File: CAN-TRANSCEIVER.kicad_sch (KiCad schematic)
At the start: 16 parts, among them U7 ATA6561-GAQW-N

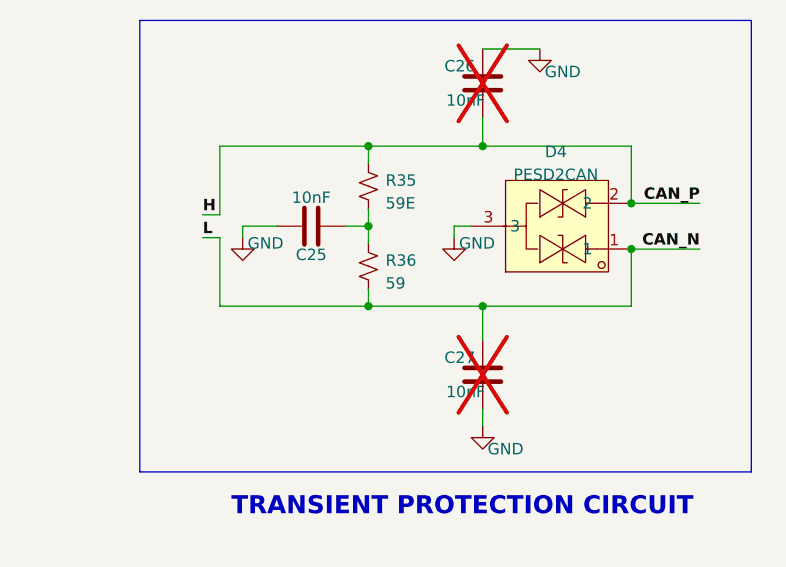
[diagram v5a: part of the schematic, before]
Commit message: Added production files for JLC (BOM and CPL)
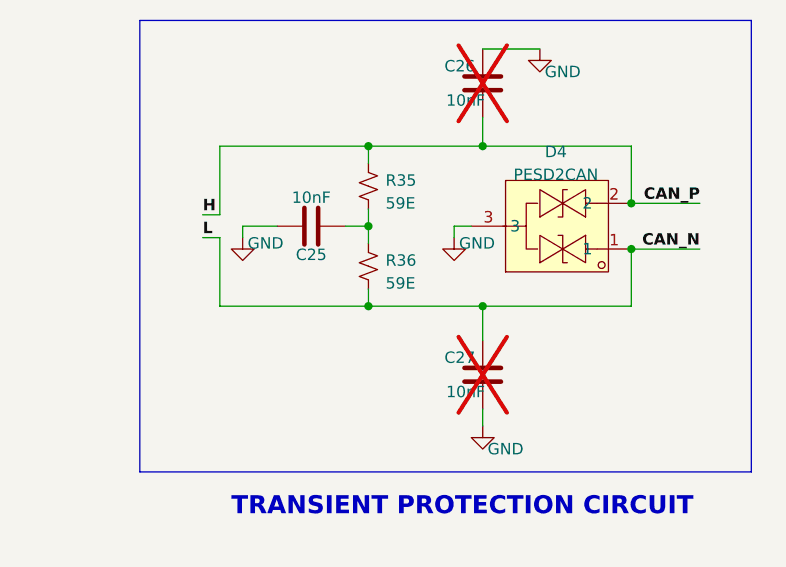
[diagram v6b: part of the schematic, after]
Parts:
- C23, C24: LCSC Part Number (none) -> C2173920
- C25: LCSC Part Number (none) -> C458948; PN CC0402KRX7R9BB103 -> MT15B103K250CT
- C26, C27: LCSC Part Number (none) -> C327415
- D4: LCSC Part Number (none) -> C284078
- R14: LCSC Part Number (none) -> C95177
- R34: LCSC Part Number (none) -> C105872
- R35: LCSC Part Number (none) -> C273340
- R36: value 59 -> 59E; LCSC Part Number (none) -> C273340
- R37, R38: LCSC Part Number (none) -> C102753
- TP3, TP4, TP6: now left out of the parts list
- U7: LCSC Part Number (none) -> C616016
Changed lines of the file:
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@@
+      (effects (font (size 1.27 1.27)) hide)
+    )
+    (property "LCSC Part Number" "C2173920" (at 166.37 110.49 0)
       (effects (font (size 1.27 1.27)) hide)
     )
@@
       (effects (font (size 1.27 1.27)) hide)
     )
+    (property "LCSC Part Number" "C2173920" (at 127.635 110.49 0)
+      (effects (font (size 1.27 1.27)) hide)
+    )
     (pin "1")
     (pin "2")
@@
   )
   (symbol (lib_id "ESP32-S3_DB:TestPoint_Alt") (at 55.245 101.6 0) (unit 1)
-    (in_bom yes) (on_board yes) (dnp no)
+    (in_bom no) (on_board yes) (dnp no)
     (property "Reference" "TP4" (at 50.8 98.425 0)
       (effects (font (size 1.27 1.27)) (justify left))
@@
       (effects (font (size 1.27 1.27)) hide)
     )
+    (property "Sim.Enable" "0" (at 55.245 101.6 0)
+      (effects (font (size 1.27 1.27)) hide)
+    )
     (pin "1")
     (instances
@@
     )
     (property "PN" "RC0402FR-075K1L" (at 165.735 92.075 0)
+      (effects (font (size 1.27 1.27)) hide)
+    )
+    (property "LCSC Part Number" "C105872" (at 165.735 92.075 0)
       (effects (font (size 1.27 1.27)) hide)
     )
@@
       (effects (font (size 1.27 1.27)) hide)
     )
+    (property "LCSC Part Number" "C327415" (at 239.395 80.645 0)
+      (effects (font (size 1.27 1.27)) hide)
+    )
     (pin "1")
     (pin "2")
@@
       (effects (font (size 1.27 1.27)) hide)
     )
+    (property "LCSC Part Number" "C95177" (at 123.825 100.965 0)
+      (effects (font (size 1.27 1.27)) hide)
+    )
     (pin "1")
     (pin "2")
@@
   )
   (symbol (lib_id "ESP32-S3_DB:TestPoint_Alt") (at 48.895 84.455 0) (unit 1)
-    (in_bom yes) (on_board yes) (dnp no)
+    (in_bom no) (on_board yes) (dnp no)
     (property "Reference" "TP6" (at 44.45 81.28 0)
       (effects (font (size 1.27 1.27)) (justify left))
@@
       (effects (font (size 1.27 1.27)) hide)
     )
+    (property "Sim.Enable" "0" (at 48.895 84.455 0)
+      (effects (font (size 1.27 1.27)) hide)
+    )
     (pin "1")
     (instances
@@
         (path "/b7fc4bd3-c219-4455-832b-8d795385dcf1/5968696a-d1c3-4df1-9868-cceeab327a7d"
           (reference "#PWR039") (unit 1)
-        )
-      )
-    )
-  )
-  (symbol (lib_id "ESP32-S3_DB:R_Small_US") (at 226.695 100.965 180) (unit 1)
-    (in_bom yes) (on_board yes) (dnp no) (fields_autoplaced)
-    (property "Reference" "R36" (at 228.6 100.33 0)
-      (effects (font (size 1.27 1.27)) (justify right))
-    )
-    (property "Value" "59" (at 228.6 102.87 0)
-      (effects (font (size 1.27 1.27)) (justify right))
-    )
-    (property "Footprint" "ESP32-S3_Dev_Board:R_0402_1005Metric" (at 226.695 100.965 0)
-      (effects (font (size 1.27 1.27)) hide)
-    )
-    (property "Datasheet" "~" (at 226.695 100.965 0)
-      (effects (font (size 1.27 1.27)) hide)
-    )
-    (property "PN" "RC0402FR-0759RL" (at 226.695 100.965 0)
-      (effects (font (size 1.27 1.27)) hide)
-    )
-    (pin "1")
-    (pin "2")
-    (instances
-      (project "ESP32-S3_DB"
-        (path "/b7fc4bd3-c219-4455-832b-8d795385dcf1/5968696a-d1c3-4df1-9868-cceeab327a7d"
-          (reference "R36") (unit 1)
         )
       )
@@
     )
     (property "PN" "ATA6561-GAQW-N" (at 134.62 95.885 0)
+      (effects (font (size 1.27 1.27)) hide)
+    )
+    (property "LCSC Part Number" "C616016" (at 134.62 95.885 0)
       (effects (font (size 1.27 1.27)) hide)
     )
@@
       (effects (font (size 1.27 1.27)) hide)
     )
+    (property "LCSC Part Number" "C284078" (at 248.285 96.52 0)
+      (effects (font (size 1.27 1.27)) hide)
+    )
     (pin "1")
     (pin "2")
@@
     )
   )
+  (symbol (lib_id "ESP32-S3_DB:R_Small_US") (at 226.695 100.965 180) (unit 1)
+    (in_bom yes) (on_board yes) (dnp no) (fields_autoplaced)
+    (property "Reference" "R36" (at 228.6 100.33 0)
+      (effects (font (size 1.27 1.27)) (justify right))
+    )
+    (property "Value" "59E" (at 228.6 102.87 0)
+      (effects (font (size 1.27 1.27)) (justify right))
+    )
+    (property "Footprint" "ESP32-S3_Dev_Board:R_0402_1005Metric" (at 226.695 100.965 0)
+      (effects (font (size 1.27 1.27)) hide)
+    )
+    (property "Datasheet" "~" (at 226.695 100.965 0)
+      (effects (font (size 1.27 1.27)) hide)
+    )
+    (property "PN" "RC0402FR-0759RL" (at 226.695 100.965 0)
+      (effects (font (size 1.27 1.27)) hide)
+    )
+    (property "LCSC Part Number" "C273340" (at 226.695 100.965 0)
+      (effects (font (size 1.27 1.27)) hide)
+    )
+    (pin "1")
+    (pin "2")
+    (instances
+      (project "ESP32-S3_DB"
+        (path "/b7fc4bd3-c219-4455-832b-8d795385dcf1/5968696a-d1c3-4df1-9868-cceeab327a7d"
+          (reference "R36") (unit 1)
+        )
+      )
+    )
+  )
   (symbol (lib_id "ESP32-S3_DB:TestPoint_Alt") (at 55.245 95.25 0) (unit 1)
-    (in_bom yes) (on_board yes) (dnp no)
+    (in_bom no) (on_board yes) (dnp no)
     (property "Reference" "TP3" (at 50.8 92.075 0)
       (effects (font (size 1.27 1.27)) (justify left))
@@
       (effects (font (size 1.27 1.27)) hide)
     )
+    (property "Sim.Enable" "0" (at 55.245 95.25 0)
+      (effects (font (size 1.27 1.27)) hide)
+    )
     (pin "1")
     (instances
@@
       (effects (font (size 1.27 1.27)) hide)
     )
+    (property "LCSC Part Number" "C102753" (at 66.04 101.6 0)
+      (effects (font (size 1.27 1.27)) hide)
+    )
     (pin "1")
     (pin "2")
@@
     )
     (property "PN" "RTT02100JTH" (at 66.04 95.25 0)
+      (effects (font (size 1.27 1.27)) hide)
+    )
+    (property "LCSC Part Number" "C102753" (at 66.04 95.25 0)
       (effects (font (size 1.27 1.27)) hide)
     )
@@
       (effects (font (size 1.27 1.27)) hide)
     )
+    (property "LCSC Part Number" "C273340" (at 226.695 92.075 0)
+      (effects (font (size 1.27 1.27)) hide)
+    )
     (pin "1")
     (pin "2")
@@
       (effects (font (size 1.27 1.27)) hide)
     )
-    (property "PN" "CC0402KRX7R9BB103" (at 220.345 96.52 0)
+    (property "PN" "MT15B103K250CT" (at 220.345 96.52 0)
+      (effects (font (size 1.27 1.27)) hide)
+    )
+    (property "LCSC Part Number" "C458948" (at 220.345 96.52 0)
       (effects (font (size 1.27 1.27)) hide)
     )
@@
       (effects (font (size 1.27 1.27)) hide)
     )
+    (property "LCSC Part Number" "C327415" (at 239.395 113.03 0)
+      (effects (font (size 1.27 1.27)) hide)
+    )
